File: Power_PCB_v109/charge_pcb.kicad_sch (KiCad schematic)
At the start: 48 parts, among them J1 Mow3, J10 Mot_Left, J11 DC/DC1, J12 DC/DC2, J2 Main_PCB1, J3 Mow2, J4 Battery, J5 Main_PCB2, J6 Power Switch, J7 Mow1, J8 Mot_Right, J9 Start, Q1 BC547C, Q2 IRF9540N, Q3 BC547C, Q4 IRF9540N, U1 INA226, U2 INA226, U3 INA226, U4 INA226, U5 INA226, U6 INA226

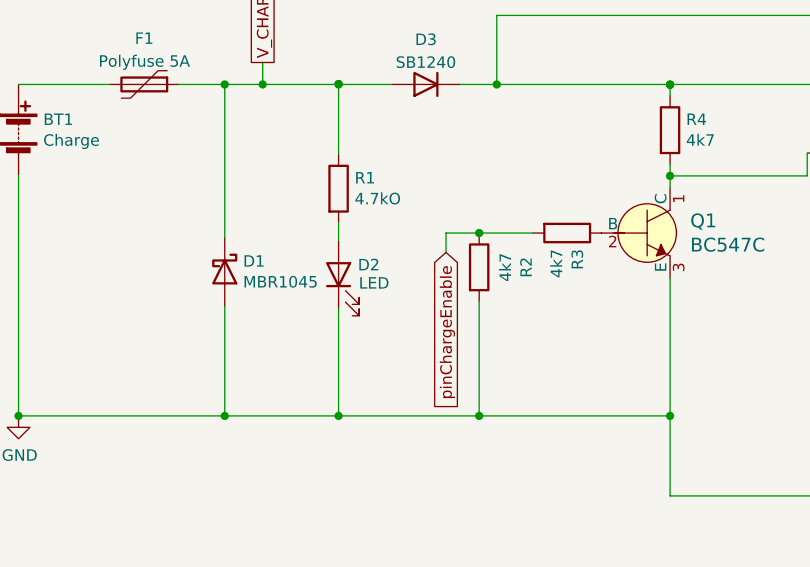
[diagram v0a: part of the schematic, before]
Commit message: Update PDF, Picture, Route
Update the PDF File of the Board.
Update PCB Picture.
Route the PCB
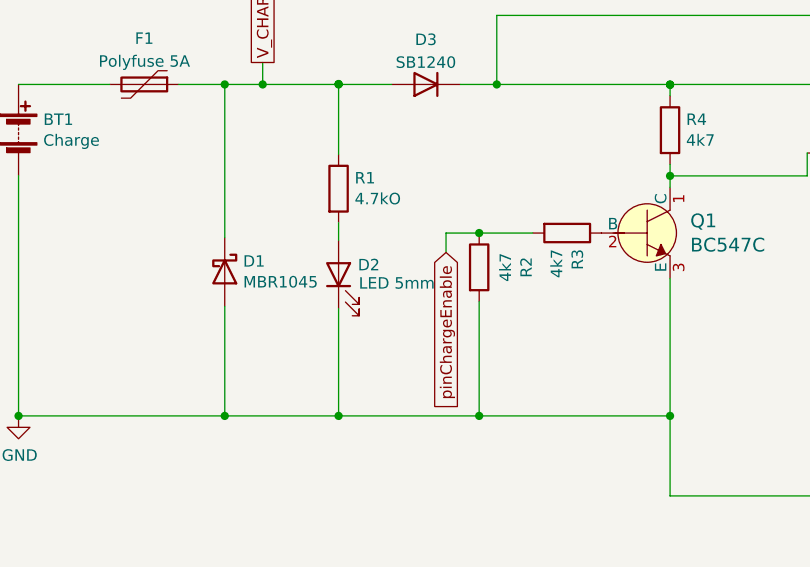
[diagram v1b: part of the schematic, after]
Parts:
- D2: value LED -> LED 5mm
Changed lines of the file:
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@@
       (effects (font (size 1.27 1.27)) (justify right))
     )
-    (property "Value" "LED" (id 1) (at 53.0352 58.928 90)
+    (property "Value" "LED 5mm" (id 1) (at 53.0352 58.928 90)
       (effects (font (size 1.27 1.27)) (justify right))
     )
@@
     )
     (path "/00000000-0000-0000-0000-00006073c265"
-      (reference "D2") (unit 1) (value "LED") (footprint "LED_THT:LED_D1.8mm_W3.3mm_H2.4mm")
+      (reference "D2") (unit 1) (value "LED 5mm") (footprint "LED_THT:LED_D1.8mm_W3.3mm_H2.4mm")
     )
     (path "/069524d1-a3ab-4e3d-9f78-5590c2ce50ad"

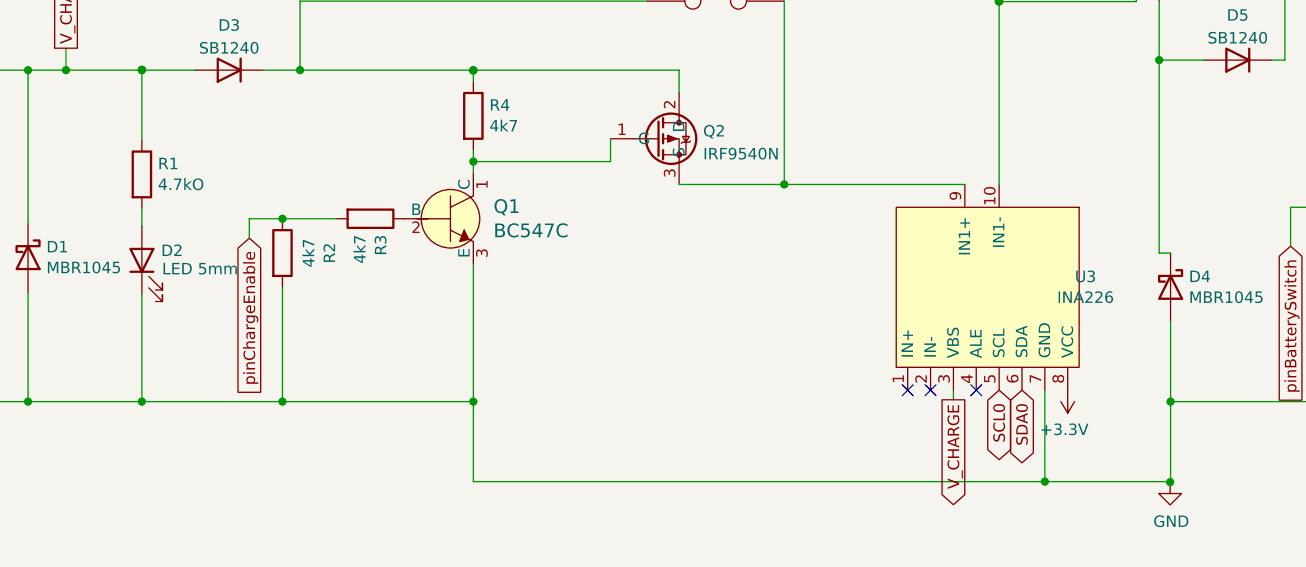
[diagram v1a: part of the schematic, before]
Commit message: Add some Logos to PCB
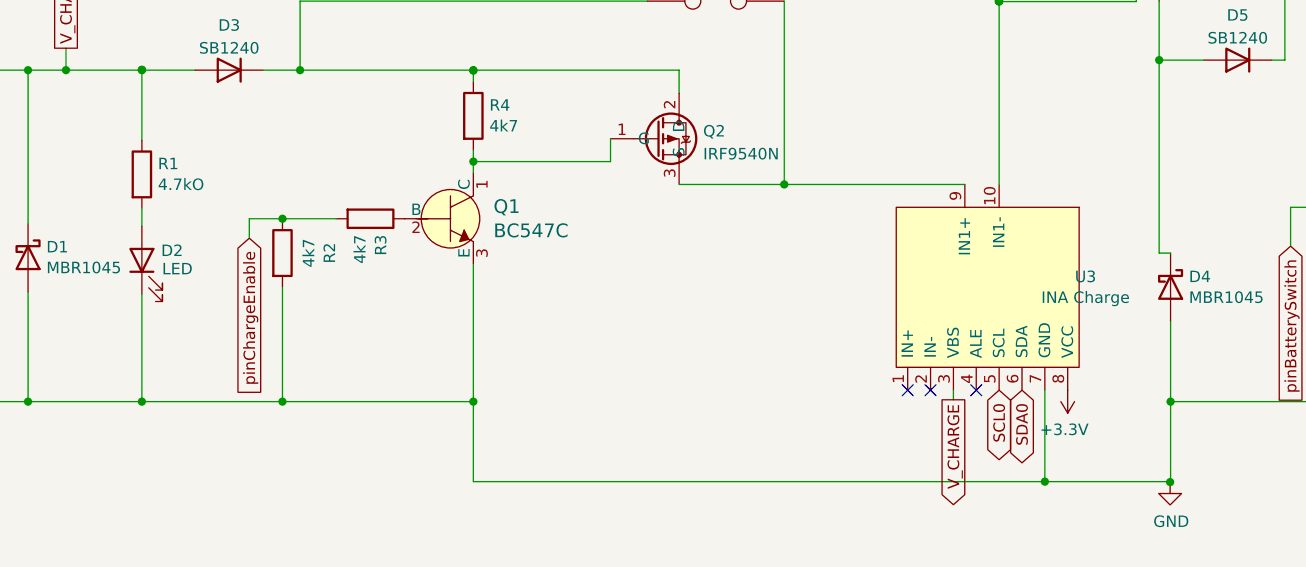
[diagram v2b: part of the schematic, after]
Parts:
- D2: value LED 5mm -> LED
- U3: value INA226 -> INA Charge
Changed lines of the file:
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@@
   (title_block
     (title "PowerPCB")
-    (date "2023-11-09")
+    (date "2023-12-05")
     (rev "v1.09")
     (comment 1 "Redesign by S.D original by Bernard")
@@
       (effects (font (size 1.27 1.27)) (justify right))
     )
-    (property "Value" "LED 5mm" (id 1) (at 53.0352 58.928 90)
+    (property "Value" "LED" (id 1) (at 53.0352 58.928 90)
       (effects (font (size 1.27 1.27)) (justify right))
     )
@@
     (in_bom yes) (on_board yes)
     (property "Reference" "U3" (id 0) (at 155.6512 59.7916 90))
-    (property "Value" "INA226" (id 1) (at 155.6512 62.103 90))
+    (property "Value" "INA Charge" (id 1) (at 155.6512 62.103 90))
     (property "Footprint" "Current_sense:INA226" (id 2) (at 133.35 60.96 0)
       (effects (font (size 1.27 1.27)) hide)
@@
     )
     (path "/00000000-0000-0000-0000-00006073c265"
-      (reference "D2") (unit 1) (value "LED 5mm") (footprint "LED_THT:LED_D1.8mm_W3.3mm_H2.4mm")
+      (reference "D2") (unit 1) (value "LED") (footprint "LED_THT:LED_D1.8mm_W3.3mm_H2.4mm")
     )
     (path "/069524d1-a3ab-4e3d-9f78-5590c2ce50ad"
@@
     )
     (path "/00000000-0000-0000-0000-000060ef0e1b"
-      (reference "U3") (unit 1) (value "INA226") (footprint "Current_sense:INA226")
+      (reference "U3") (unit 1) (value "INA Charge") (footprint "Current_sense:INA226")
     )
     (path "/00000000-0000-0000-0000-0000610169e3"

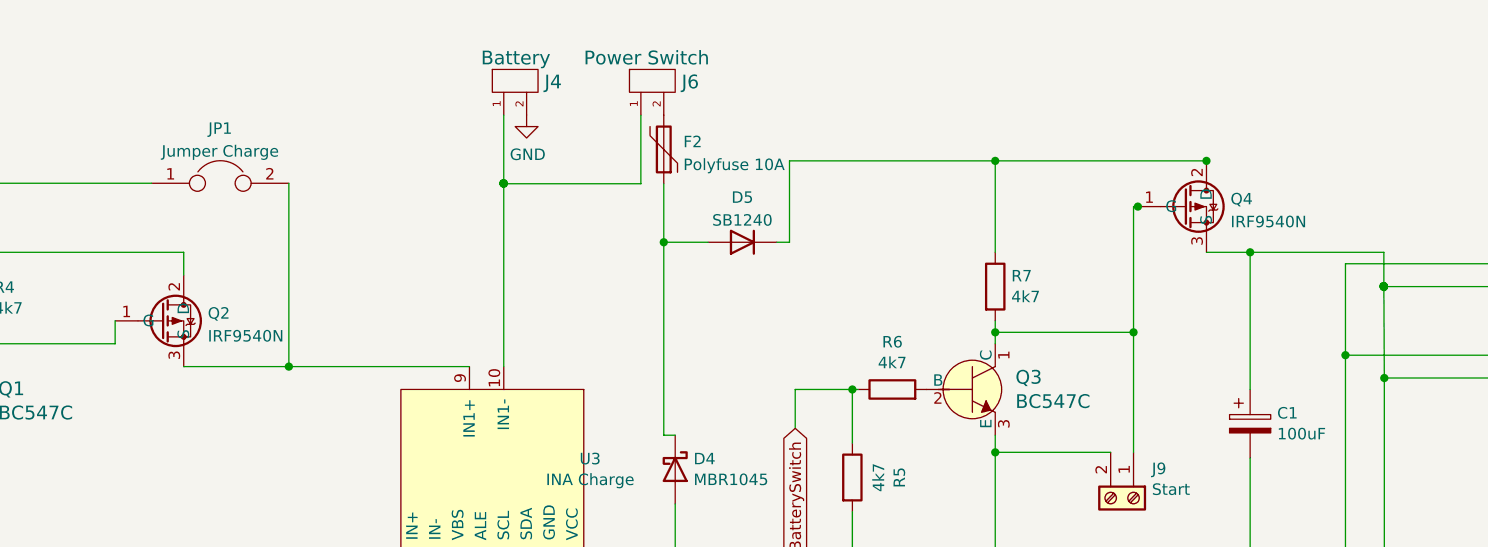
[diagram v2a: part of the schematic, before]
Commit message: Wrong Direktion of Q2 and Q4
The Drain and Source Pin was in the wrong direction.
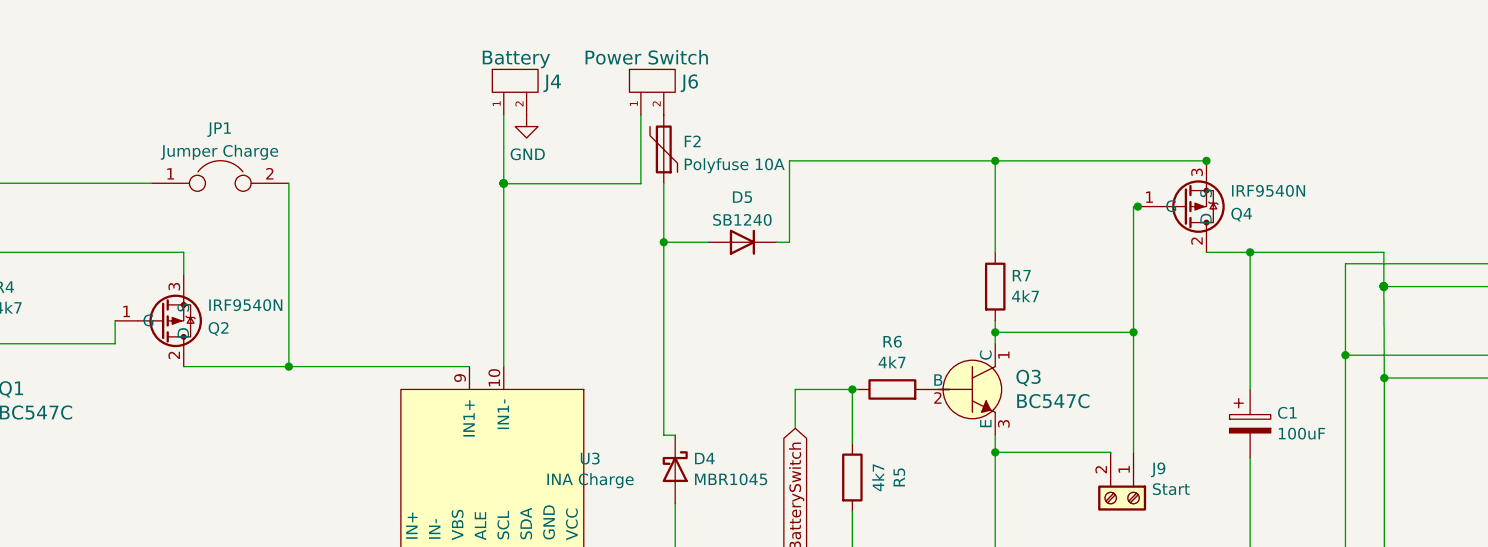
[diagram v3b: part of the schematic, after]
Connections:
- net V_Bat: now also Q4.2 (D); no longer Q4.3 (S)
- net at D3.1 (K), JP1.1, R4.1: now also Q2.3 (S); no longer Q2.2 (D)
- net at D5.1 (K), R7.1: now also Q4.3 (S); no longer Q4.2 (D)
- net at JP1.2, U3.9 (IN1+): now also Q2.2 (D); no longer Q2.3 (S)
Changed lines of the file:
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@@
   (title_block
     (title "PowerPCB")
-    (date "2023-12-05")
-    (rev "v1.09")
+    (date "2024-02-07")
+    (rev "v1.09.1")
     (comment 1 "Redesign by S.D original by Bernard")
     (comment 2 "Designed for TeensyMower")
@@
     (pin "2")
   )
-  (symbol (lib_name "IRF9540N_2") (lib_id "Transistor_FET:IRF9540N") (at 107.95 44.45 0) (unit 1)
+  (symbol (lib_name "IRF9540N_2") (lib_id "Transistor_FET:IRF9540N") (at 107.95 44.45 0) (mirror x) (unit 1)
     (in_bom yes) (on_board yes) (fields_autoplaced)
-    (property "Reference" "Q2" (id 0) (at 113.157 43.6153 0)
-      (effects (font (size 1.27 1.27)) (justify left))
-    )
-    (property "Value" "IRF9540N" (id 1) (at 113.157 46.1522 0)
-      (effects (font (size 1.27 1.27)) (justify left))
-    )
-    (property "Footprint" "Package_TO_SOT_THT:TO-220-3_Vertical" (id 2) (at 113.03 46.355 0)
+    (property "Reference" "Q2" (id 0) (at 113.157 45.2847 0)
+      (effects (font (size 1.27 1.27)) (justify left))
+    )
+    (property "Value" "IRF9540N" (id 1) (at 113.157 42.7478 0)
+      (effects (font (size 1.27 1.27)) (justify left))
+    )
+    (property "Footprint" "Package_TO_SOT_THT:TO-220-3_Vertical" (id 2) (at 113.03 42.545 0)
       (effects (font (size 1.27 1.27) italic) (justify left) hide)
     )
@@
     (pin "2")
   )
-  (symbol (lib_name "IRF9540N_2") (lib_id "Transistor_FET:IRF9540N") (at 221.5896 31.75 0) (unit 1)
+  (symbol (lib_name "IRF9540N_2") (lib_id "Transistor_FET:IRF9540N") (at 221.5896 31.75 0) (mirror x) (unit 1)
     (in_bom yes) (on_board yes) (fields_autoplaced)
-    (property "Reference" "Q4" (id 0) (at 226.7966 30.9153 0)
-      (effects (font (size 1.27 1.27)) (justify left))
-    )
-    (property "Value" "IRF9540N" (id 1) (at 226.7966 33.4522 0)
-      (effects (font (size 1.27 1.27)) (justify left))
-    )
-    (property "Footprint" "Package_TO_SOT_THT:TO-220-3_Vertical" (id 2) (at 226.6696 33.655 0)
+    (property "Reference" "Q4" (id 0) (at 226.7966 32.5847 0)
+      (effects (font (size 1.27 1.27)) (justify left))
+    )
+    (property "Value" "IRF9540N" (id 1) (at 226.7966 30.0478 0)
+      (effects (font (size 1.27 1.27)) (justify left))
+    )
+    (property "Footprint" "Package_TO_SOT_THT:TO-220-3_Vertical" (id 2) (at 226.6696 29.845 0)
       (effects (font (size 1.27 1.27) italic) (justify left) hide)
     )
